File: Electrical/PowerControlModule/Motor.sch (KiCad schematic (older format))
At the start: 7 parts, among them J1 178.6164.0002, J2 178.6164.0002, J3 178.6164.0002, J4 178.6164.0002

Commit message: Adds new part library for SCR stuff. Gets buck converters and connectors to show up on PCB layout
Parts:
- CONN10, CONN9: footprint (none) -> Connector_PinHeader_2.54mm:PinHeader_1x02_P2.54mm_Vertical
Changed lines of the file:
@@
 $Descr A4 11693 8268
 encoding utf-8
-Sheet 10 11
+Sheet 11 11
 Title ""
 Date ""
@@
 F 0 "CONN12" H 6030 5092 50  0000 L CNN
 F 1 "Conn_01x02" H 6030 5001 50  0000 L CNN
-F 2 "" H 5950 5100 50  0001 C CNN
+F 2 "Connector_PinHeader_2.54mm:PinHeader_1x02_P2.54mm_Vertical" H 5950 5100 50  0001 C CNN
 F 3 "~" H 5950 5100 50  0001 C CNN
 	1    5950 5100
@@
 F 0 "CONN11" H 5030 5092 50  0000 L CNN
 F 1 "Conn_01x02" H 5030 5001 50  0000 L CNN
-F 2 "" H 4950 5100 50  0001 C CNN
+F 2 "Connector_PinHeader_2.54mm:PinHeader_1x02_P2.54mm_Vertical" H 4950 5100 50  0001 C CNN
 F 3 "~" H 4950 5100 50  0001 C CNN
 	1    4950 5100

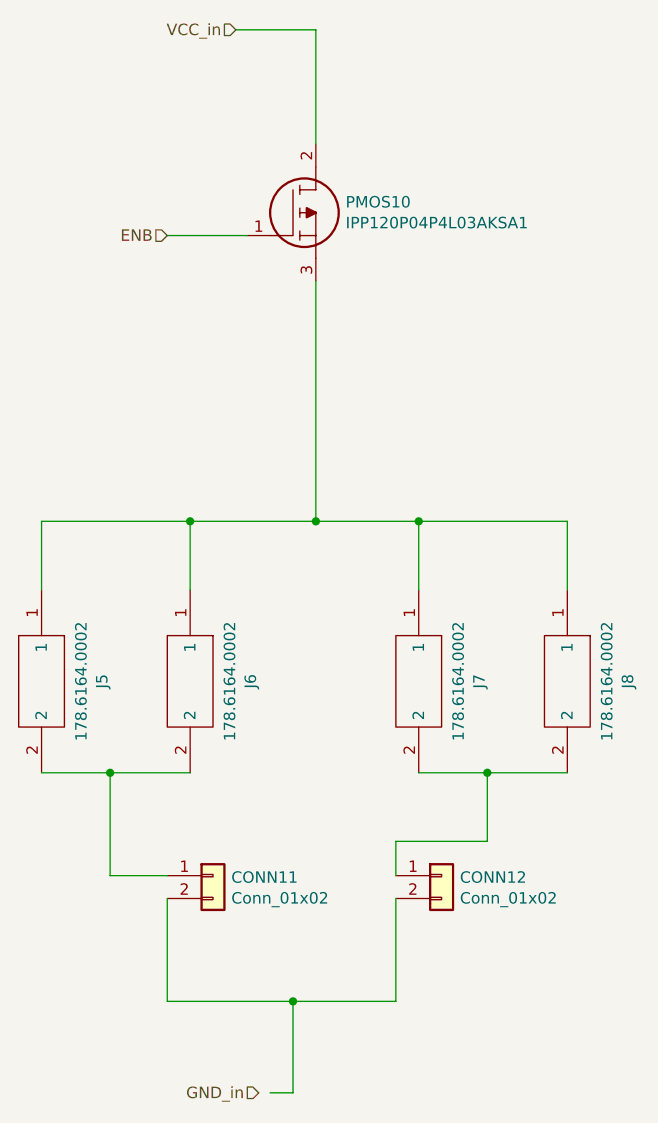
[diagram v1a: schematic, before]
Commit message: Lays out power distribution board on PCB. Need to make 4 layer setup before routing. Also need to change motor output footprint
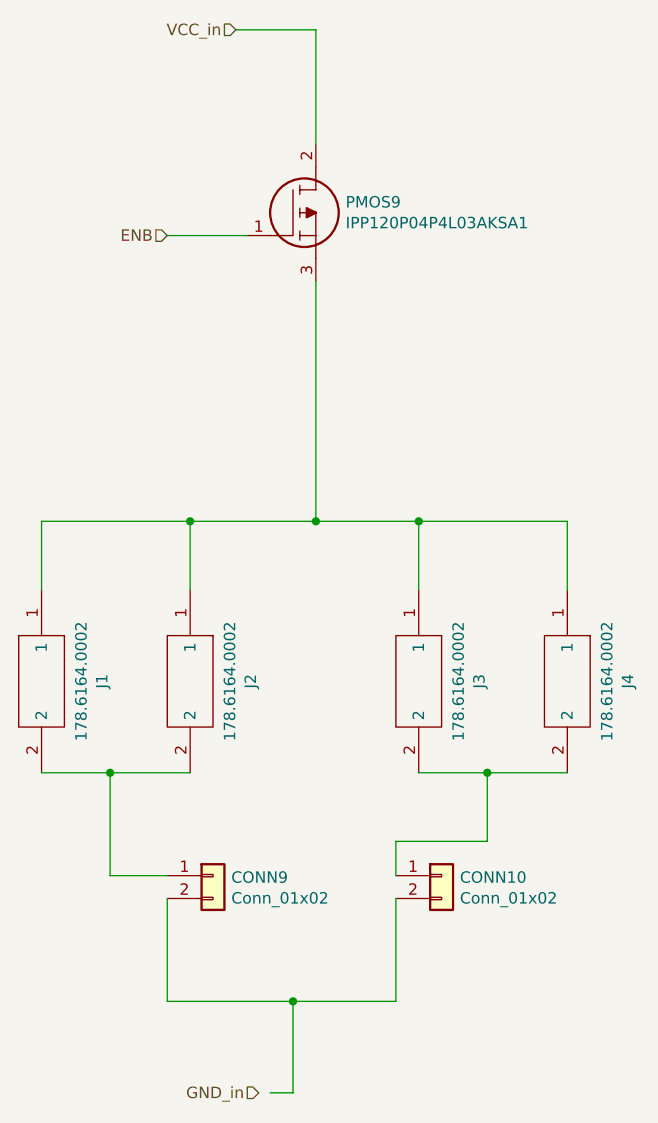
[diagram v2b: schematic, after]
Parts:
- CONN10, CONN9: footprint Connector_PinHeader_2.54mm:PinHeader_1x02_P2.54mm_Vertical -> Connector_Wire:SolderWirePad_1x02_P5.08mm_Drill1.5mm
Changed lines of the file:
@@
 $Descr A4 11693 8268
 encoding utf-8
-Sheet 11 11
+Sheet 10 11
 Title ""
 Date ""
@@
 AR Path="/5D9C920E/5D9CD656" Ref="PMOS9"  Part="1"
 AR Path="/5D9D6498/5D9CD656" Ref="PMOS10"  Part="1"
-F 0 "PMOS10" H 5530 2446 50  0000 L CNN
+F 0 "PMOS9" H 5530 2446 50  0000 L CNN
 F 1 "IPP120P04P4L03AKSA1" H 5530 2355 50  0000 L CNN
 F 2 "LibraryLoader:TO254P440X1000X2110-3P" H 5550 2250 50  0001 L CNN
@@
 AR Path="/5D9C920E/5D9CD66A" Ref="J4"  Part="1"
 AR Path="/5D9D6498/5D9CD66A" Ref="J8"  Part="1"
-F 0 "J8" H 6900 4115 50  0000 C CNN
+F 0 "J4" H 6900 4115 50  0000 C CNN
 F 1 "178.6164.0002" H 6900 4024 50  0000 C CNN
 F 2 "LibraryLoader:178.6164.0002_1" H 7150 3950 50  0001 L CNN
@@
 AR Path="/5D9C920E/5D9CD676" Ref="J3"  Part="1"
 AR Path="/5D9D6498/5D9CD676" Ref="J7"  Part="1"
-F 0 "J7" H 6250 4115 50  0000 C CNN
+F 0 "J3" H 6250 4115 50  0000 C CNN
 F 1 "178.6164.0002" H 6250 4024 50  0000 C CNN
 F 2 "LibraryLoader:178.6164.0002_1" H 6500 3950 50  0001 L CNN
@@
 AR Path="/5D9C920E/5D9CD682" Ref="J2"  Part="1"
 AR Path="/5D9D6498/5D9CD682" Ref="J6"  Part="1"
-F 0 "J6" H 5250 4115 50  0000 C CNN
+F 0 "J2" H 5250 4115 50  0000 C CNN
 F 1 "178.6164.0002" H 5250 4024 50  0000 C CNN
 F 2 "LibraryLoader:178.6164.0002_1" H 5500 3950 50  0001 L CNN
@@
 AR Path="/5D9C920E/5D9CD68E" Ref="J1"  Part="1"
 AR Path="/5D9D6498/5D9CD68E" Ref="J5"  Part="1"
-F 0 "J5" H 4600 4115 50  0000 C CNN
+F 0 "J1" H 4600 4115 50  0000 C CNN
 F 1 "178.6164.0002" H 4600 4024 50  0000 C CNN
 F 2 "LibraryLoader:178.6164.0002_1" H 4850 3950 50  0001 L CNN
@@
 AR Path="/5D9C920E/5D9CD6A3" Ref="CONN10"  Part="1"
 AR Path="/5D9D6498/5D9CD6A3" Ref="CONN12"  Part="1"
-F 0 "CONN12" H 6030 5092 50  0000 L CNN
+F 0 "CONN10" H 6030 5092 50  0000 L CNN
 F 1 "Conn_01x02" H 6030 5001 50  0000 L CNN
-F 2 "Connector_PinHeader_2.54mm:PinHeader_1x02_P2.54mm_Vertical" H 5950 5100 50  0001 C CNN
+F 2 "Connector_Wire:SolderWirePad_1x02_P5.08mm_Drill1.5mm" H 5950 5100 50  0001 C CNN
 F 3 "~" H 5950 5100 50  0001 C CNN
 	1    5950 5100
@@
 AR Path="/5D9C920E/5D9CD6AB" Ref="CONN9"  Part="1"
 AR Path="/5D9D6498/5D9CD6AB" Ref="CONN11"  Part="1"
-F 0 "CONN11" H 5030 5092 50  0000 L CNN
+F 0 "CONN9" H 5030 5092 50  0000 L CNN
 F 1 "Conn_01x02" H 5030 5001 50  0000 L CNN
-F 2 "Connector_PinHeader_2.54mm:PinHeader_1x02_P2.54mm_Vertical" H 4950 5100 50  0001 C CNN
+F 2 "Connector_Wire:SolderWirePad_1x02_P5.08mm_Drill1.5mm" H 4950 5100 50  0001 C CNN
 F 3 "~" H 4950 5100 50  0001 C CNN
 	1    4950 5100

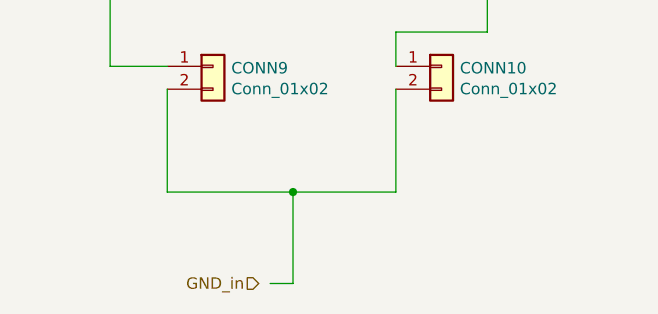
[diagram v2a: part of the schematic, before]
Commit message: Fixes silkscreen stuff and adds ground connection for motor control battery connection
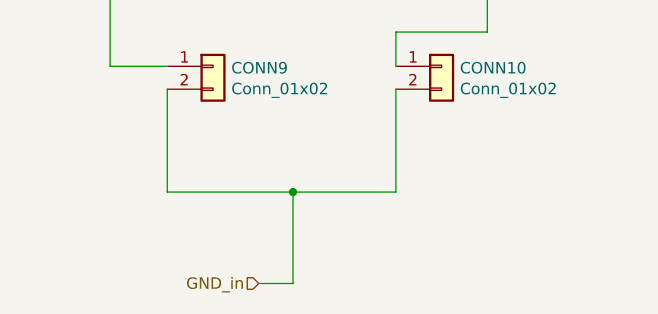
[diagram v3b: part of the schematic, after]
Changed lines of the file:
@@
 GND_in
-Wire Wire Line
-	5200 6050 5300 6050
 Wire Wire Line
 	5300 6050 5300 5650
@@
 Wire Wire Line
 	4750 5650 5300 5650
+Wire Wire Line
+	5150 6050 5300 6050
 $EndSCHEMATC

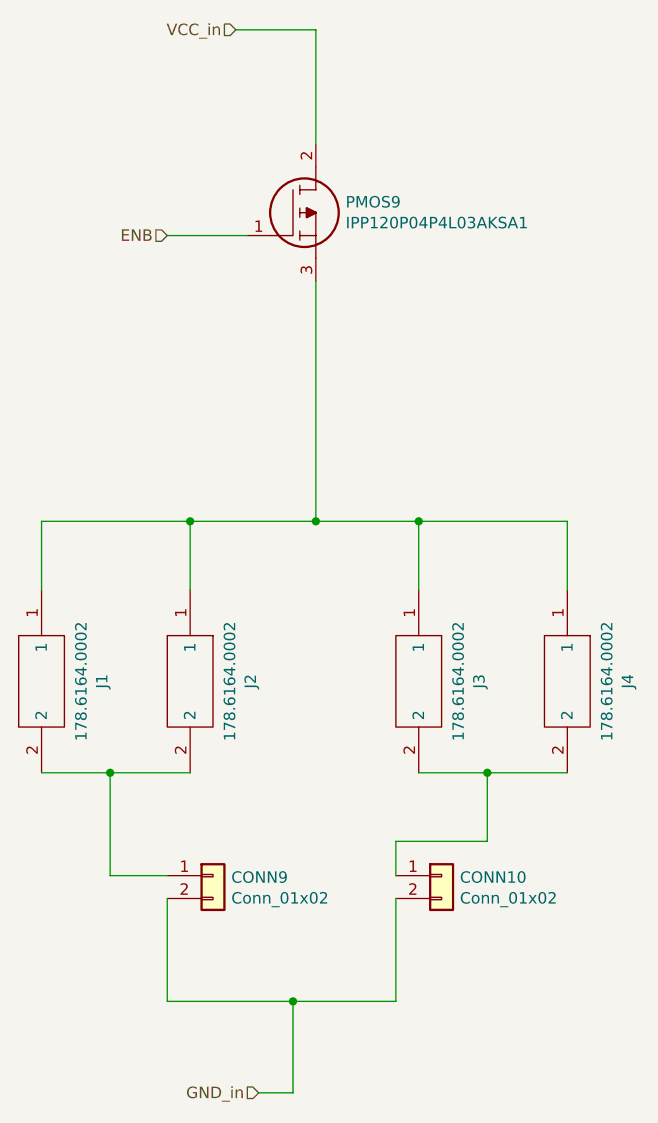
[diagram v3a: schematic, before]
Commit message: Peripheral changes and rewired PCB
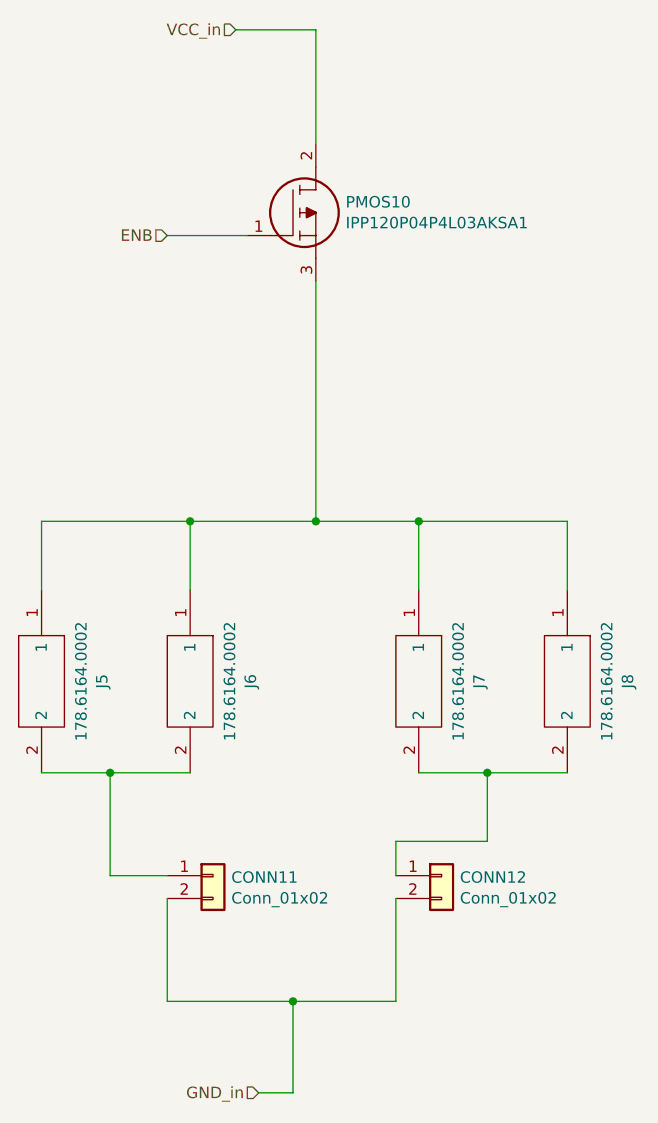
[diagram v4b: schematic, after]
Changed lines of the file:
@@
 $Descr A4 11693 8268
 encoding utf-8
-Sheet 10 11
+Sheet 11 11
 Title ""
 Date ""
@@
 AR Path="/5D9C920E/5D9CD656" Ref="PMOS9"  Part="1"
 AR Path="/5D9D6498/5D9CD656" Ref="PMOS10"  Part="1"
-F 0 "PMOS9" H 5530 2446 50  0000 L CNN
+F 0 "PMOS10" H 5530 2446 50  0000 L CNN
 F 1 "IPP120P04P4L03AKSA1" H 5530 2355 50  0000 L CNN
 F 2 "LibraryLoader:TO254P440X1000X2110-3P" H 5550 2250 50  0001 L CNN
@@
 AR Path="/5D9C920E/5D9CD66A" Ref="J4"  Part="1"
 AR Path="/5D9D6498/5D9CD66A" Ref="J8"  Part="1"
-F 0 "J4" H 6900 4115 50  0000 C CNN
+F 0 "J8" H 6900 4115 50  0000 C CNN
 F 1 "178.6164.0002" H 6900 4024 50  0000 C CNN
 F 2 "LibraryLoader:178.6164.0002_1" H 7150 3950 50  0001 L CNN
@@
 AR Path="/5D9C920E/5D9CD676" Ref="J3"  Part="1"
 AR Path="/5D9D6498/5D9CD676" Ref="J7"  Part="1"
-F 0 "J3" H 6250 4115 50  0000 C CNN
+F 0 "J7" H 6250 4115 50  0000 C CNN
 F 1 "178.6164.0002" H 6250 4024 50  0000 C CNN
 F 2 "LibraryLoader:178.6164.0002_1" H 6500 3950 50  0001 L CNN
@@
 AR Path="/5D9C920E/5D9CD682" Ref="J2"  Part="1"
 AR Path="/5D9D6498/5D9CD682" Ref="J6"  Part="1"
-F 0 "J2" H 5250 4115 50  0000 C CNN
+F 0 "J6" H 5250 4115 50  0000 C CNN
 F 1 "178.6164.0002" H 5250 4024 50  0000 C CNN
 F 2 "LibraryLoader:178.6164.0002_1" H 5500 3950 50  0001 L CNN
@@
 AR Path="/5D9C920E/5D9CD68E" Ref="J1"  Part="1"
 AR Path="/5D9D6498/5D9CD68E" Ref="J5"  Part="1"
-F 0 "J1" H 4600 4115 50  0000 C CNN
+F 0 "J5" H 4600 4115 50  0000 C CNN
 F 1 "178.6164.0002" H 4600 4024 50  0000 C CNN
 F 2 "LibraryLoader:178.6164.0002_1" H 4850 3950 50  0001 L CNN
@@
 AR Path="/5D9C920E/5D9CD6A3" Ref="CONN10"  Part="1"
 AR Path="/5D9D6498/5D9CD6A3" Ref="CONN12"  Part="1"
-F 0 "CONN10" H 6030 5092 50  0000 L CNN
+F 0 "CONN12" H 6030 5092 50  0000 L CNN
 F 1 "Conn_01x02" H 6030 5001 50  0000 L CNN
 F 2 "Connector_Wire:SolderWirePad_1x02_P5.08mm_Drill1.5mm" H 5950 5100 50  0001 C CNN
@@
 AR Path="/5D9C920E/5D9CD6AB" Ref="CONN9"  Part="1"
 AR Path="/5D9D6498/5D9CD6AB" Ref="CONN11"  Part="1"
-F 0 "CONN9" H 5030 5092 50  0000 L CNN
+F 0 "CONN11" H 5030 5092 50  0000 L CNN
 F 1 "Conn_01x02" H 5030 5001 50  0000 L CNN
 F 2 "Connector_Wire:SolderWirePad_1x02_P5.08mm_Drill1.5mm" H 4950 5100 50  0001 C CNN

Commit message: Splits project into multiple modules, peripherals, motors, and safety
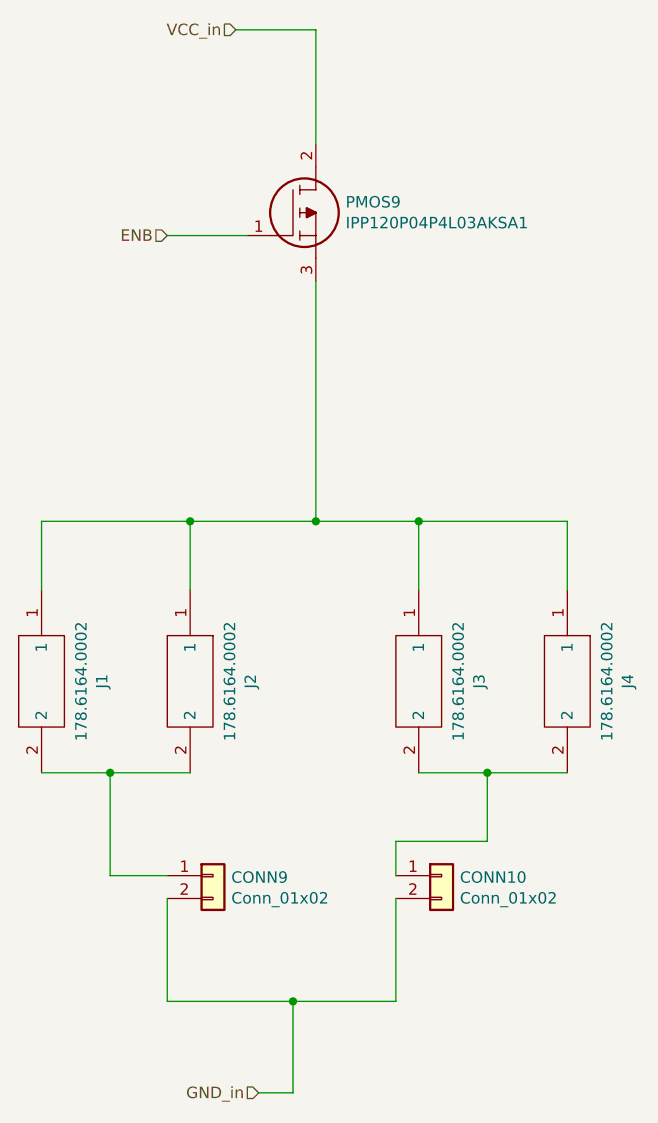
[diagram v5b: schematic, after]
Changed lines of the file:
@@
 $Descr A4 11693 8268
 encoding utf-8
-Sheet 11 11
+Sheet 10 11
 Title ""
 Date ""
@@
 AR Path="/5D9C920E/5D9CD656" Ref="PMOS9"  Part="1"
 AR Path="/5D9D6498/5D9CD656" Ref="PMOS10"  Part="1"
-F 0 "PMOS10" H 5530 2446 50  0000 L CNN
+F 0 "PMOS9" H 5530 2446 50  0000 L CNN
 F 1 "IPP120P04P4L03AKSA1" H 5530 2355 50  0000 L CNN
 F 2 "LibraryLoader:TO254P440X1000X2110-3P" H 5550 2250 50  0001 L CNN
@@
 AR Path="/5D9C920E/5D9CD66A" Ref="J4"  Part="1"
 AR Path="/5D9D6498/5D9CD66A" Ref="J8"  Part="1"
-F 0 "J8" H 6900 4115 50  0000 C CNN
+F 0 "J4" H 6900 4115 50  0000 C CNN
 F 1 "178.6164.0002" H 6900 4024 50  0000 C CNN
 F 2 "LibraryLoader:178.6164.0002_1" H 7150 3950 50  0001 L CNN
@@
 AR Path="/5D9C920E/5D9CD676" Ref="J3"  Part="1"
 AR Path="/5D9D6498/5D9CD676" Ref="J7"  Part="1"
-F 0 "J7" H 6250 4115 50  0000 C CNN
+F 0 "J3" H 6250 4115 50  0000 C CNN
 F 1 "178.6164.0002" H 6250 4024 50  0000 C CNN
 F 2 "LibraryLoader:178.6164.0002_1" H 6500 3950 50  0001 L CNN
@@
 AR Path="/5D9C920E/5D9CD682" Ref="J2"  Part="1"
 AR Path="/5D9D6498/5D9CD682" Ref="J6"  Part="1"
-F 0 "J6" H 5250 4115 50  0000 C CNN
+F 0 "J2" H 5250 4115 50  0000 C CNN
 F 1 "178.6164.0002" H 5250 4024 50  0000 C CNN
 F 2 "LibraryLoader:178.6164.0002_1" H 5500 3950 50  0001 L CNN
@@
 AR Path="/5D9C920E/5D9CD68E" Ref="J1"  Part="1"
 AR Path="/5D9D6498/5D9CD68E" Ref="J5"  Part="1"
-F 0 "J5" H 4600 4115 50  0000 C CNN
+F 0 "J1" H 4600 4115 50  0000 C CNN
 F 1 "178.6164.0002" H 4600 4024 50  0000 C CNN
 F 2 "LibraryLoader:178.6164.0002_1" H 4850 3950 50  0001 L CNN
@@
 AR Path="/5D9C920E/5D9CD6A3" Ref="CONN10"  Part="1"
 AR Path="/5D9D6498/5D9CD6A3" Ref="CONN12"  Part="1"
-F 0 "CONN12" H 6030 5092 50  0000 L CNN
+F 0 "CONN10" H 6030 5092 50  0000 L CNN
 F 1 "Conn_01x02" H 6030 5001 50  0000 L CNN
 F 2 "Connector_Wire:SolderWirePad_1x02_P5.08mm_Drill1.5mm" H 5950 5100 50  0001 C CNN
@@
 AR Path="/5D9C920E/5D9CD6AB" Ref="CONN9"  Part="1"
 AR Path="/5D9D6498/5D9CD6AB" Ref="CONN11"  Part="1"
-F 0 "CONN11" H 5030 5092 50  0000 L CNN
+F 0 "CONN9" H 5030 5092 50  0000 L CNN
 F 1 "Conn_01x02" H 5030 5001 50  0000 L CNN
 F 2 "Connector_Wire:SolderWirePad_1x02_P5.08mm_Drill1.5mm" H 4950 5100 50  0001 C CNN
